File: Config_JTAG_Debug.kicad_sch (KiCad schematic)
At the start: 79 parts, among them J300 DigilentH2SHeader, J301 USB3100-30-A, Q100 T2N7002AK,LM, SW300 SKRPANE010, SW301 219-3LPST, U200 XC7Z010-2CLG400I, U300 FT2232HL, U301 93LC65B-I/SN, X300 ECS-2520MV-120-BN

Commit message: Finished schematic page 4: Zynq Processing System (PS), includes 128MBit QSPI flash, 33.33 MHz PS Clock, and 4Gbyte EMMC Memory
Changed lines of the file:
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@@
     (stroke (width 0) (type default))
   )
-  (wire (pts (xy 21.59 199.39) (xy 36.83 199.39))
+  (wire (pts (xy 35.56 199.39) (xy 36.83 199.39))
     (stroke (width 0) (type default))
   )
@@
     (stroke (width 0) (type default))
   )
-  (wire (pts (xy 91.44 198.12) (xy 105.41 198.12))
+  (wire (pts (xy 104.14 198.12) (xy 105.41 198.12))
     (stroke (width 0) (type default))
   )
@@
     (stroke (width 0) (type default))
   )
-  (wire (pts (xy 21.59 207.01) (xy 36.83 207.01))
+  (wire (pts (xy 35.56 207.01) (xy 36.83 207.01))
     (stroke (width 0) (type default))
   )
@@
     (stroke (width 0) (type default))
   )
-  (wire (pts (xy 21.59 191.77) (xy 36.83 191.77))
+  (wire (pts (xy 35.56 191.77) (xy 36.83 191.77))
     (stroke (width 0) (type default))
   )
@@
     (stroke (width 0) (type default))
   )
-  (wire (pts (xy 138.43 198.12) (xy 153.67 198.12))
+  (wire (pts (xy 152.4 198.12) (xy 153.67 198.12))
     (stroke (width 0) (type default))
   )
@@
     (effects (font (size 1.27 1.27)) (justify right bottom))
   )
-  (label "QSPI_DQ1_M1" (at 21.59 199.39 0) (fields_autoplaced)
-    (effects (font (size 1.27 1.27)) (justify left bottom))
-  )
   (label "M1" (at 45.72 199.39 0) (fields_autoplaced)
     (effects (font (size 1.27 1.27)) (justify left bottom))
@@
     (effects (font (size 1.27 1.27)) (justify left bottom))
   )
-  (label "QSPI_DQ3_M0" (at 21.59 191.77 0) (fields_autoplaced)
-    (effects (font (size 1.27 1.27)) (justify left bottom))
-  )
-  (label "QSPI_DQ2_M2" (at 21.59 207.01 0) (fields_autoplaced)
-    (effects (font (size 1.27 1.27)) (justify left bottom))
-  )
   (label "CLK_12MHZ" (at 238.76 229.87 0) (fields_autoplaced)
     (effects (font (size 1.27 1.27)) (justify left bottom))
@@
     (effects (font (size 1.27 1.27)) (justify left bottom))
   )
-  (label "QSPI_DQ0_M3" (at 91.44 198.12 0) (fields_autoplaced)
-    (effects (font (size 1.27 1.27)) (justify left bottom))
-  )
   (label "TCK" (at 53.34 73.66 0) (fields_autoplaced)
     (effects (font (size 1.27 1.27)) (justify left bottom))
@@
     (effects (font (size 1.27 1.27)) (justify left bottom))
   )
-  (label "FLASH_CLK_M4" (at 138.43 198.12 0) (fields_autoplaced)
-    (effects (font (size 1.27 1.27)) (justify left bottom))
-  )
   (label "JTAG_TDO" (at 153.67 71.12 0) (fields_autoplaced)
     (effects (font (size 0.762 0.762)) (justify left bottom))
@@
     (effects (font (size 1.016 1.016)) (justify left bottom))
   )
+  (global_label "QSPI_DQ1_M1" (shape input) (at 35.56 199.39 180) (fields_autoplaced)
+    (effects (font (size 1.27 1.27)) (justify right))
+    (property "Intersheetrefs" "${INTERSHEET_REFS}" (at 0 0 0)
+      (effects (font (size 1.27 1.27)) hide)
+    )
+  )
   (global_label "UART1_RX" (shape output) (at 387.35 161.29 0) (fields_autoplaced)
     (effects (font (size 1.27 1.27)) (justify left))
+    (property "Intersheetrefs" "${INTERSHEET_REFS}" (at 0 0 0)
+      (effects (font (size 1.27 1.27)) hide)
+    )
+  )
+  (global_label "FLASH_CLK_M4" (shape input) (at 152.4 198.12 180) (fields_autoplaced)
+    (effects (font (size 1.27 1.27)) (justify right))
+    (property "Intersheetrefs" "${INTERSHEET_REFS}" (at 0 0 0)
+      (effects (font (size 1.27 1.27)) hide)
+    )
+  )
+  (global_label "QSPI_DQ2_M2" (shape input) (at 35.56 207.01 180) (fields_autoplaced)
+    (effects (font (size 1.27 1.27)) (justify right))
+    (property "Intersheetrefs" "${INTERSHEET_REFS}" (at 0 0 0)
+      (effects (font (size 1.27 1.27)) hide)
+    )
+  )
+  (global_label "QSPI_DQ0_M3" (shape input) (at 104.14 198.12 180) (fields_autoplaced)
+    (effects (font (size 1.27 1.27)) (justify right))
+    (property "Intersheetrefs" "${INTERSHEET_REFS}" (at 0 0 0)
+      (effects (font (size 1.27 1.27)) hide)
+    )
+  )
+  (global_label "QSPI_DQ3_M0" (shape input) (at 35.56 191.77 180) (fields_autoplaced)
+    (effects (font (size 1.27 1.27)) (justify right))
+    (property "Intersheetrefs" "${INTERSHEET_REFS}" (at 0 0 0)
+      (effects (font (size 1.27 1.27)) hide)
+    )
   )
   (global_label "UART1_TX_VCFG1" (shape input) (at 383.54 166.37 0) (fields_autoplaced)
     (effects (font (size 1.27 1.27)) (justify left))
+    (property "Intersheetrefs" "${INTERSHEET_REFS}" (at 0 0 0)
+      (effects (font (size 1.27 1.27)) hide)
+    )
   )
   (global_label "PS_NPOR" (shape bidirectional) (at 384.81 130.81 0) (fields_autoplaced)
@@
         )
         (path "/ec71d28a-654e-4dfb-b412-dd09b7b3e4b8/b94623a7-025c-4682-97b9-752e423a938a"
-          (reference "C1") (unit 1)
+          (reference "C307") (unit 1)
         )
       )
@@
         )
         (path "/ec71d28a-654e-4dfb-b412-dd09b7b3e4b8/b94623a7-025c-4682-97b9-752e423a938a"
-          (reference "C3") (unit 1)
+          (reference "C309") (unit 1)
         )
       )
@@
         )
         (path "/ec71d28a-654e-4dfb-b412-dd09b7b3e4b8/b94623a7-025c-4682-97b9-752e423a938a"
-          (reference "C2") (unit 1)
+          (reference "C308") (unit 1)
         )
       )
@@
       (effects (font (size 1.27 1.27)) hide)
     )
+    (property "LCSC #" "" (at 29.21 227.33 0)
+      (effects (font (size 1.27 1.27)) hide)
+    )
     (pin "F6")
     (pin "F9")
@@
     (pin "R10")
     (pin "R11")
+    (pin "A10")
+    (pin "A11")
+    (pin "A12")
+    (pin "A14")
+    (pin "A15")
+    (pin "A16")
+    (pin "A17")
+    (pin "A19")
+    (pin "A5")
+    (pin "A6")
+    (pin "A7")
+    (pin "A9")
+    (pin "B10")
+    (pin "B12")
+    (pin "B13")
+    (pin "B14")
+    (pin "B15")
+    (pin "B17")
+    (pin "B18")
+    (pin "B5")
+    (pin "B7")
+    (pin "B8")
+    (pin "B9")
+    (pin "C10")
+    (pin "C11")
+    (pin "C12")
+    (pin "C13")
+    (pin "C15")
+    (pin "C16")
+    (pin "C17")
+    (pin "C18")
+    (pin "C5")
+    (pin "C6")
+    (pin "C7")
+    (pin "C8")
+    (pin "D10")
+    (pin "D11")
+    (pin "D13")
+    (pin "D14")
+    (pin "D15")
+    (pin "D16")
+    (pin "D5")
+    (pin "D6")
+    (pin "D8")
+    (pin "D9")
+    (pin "E11")
+    (pin "E12")
+    (pin "E13")
+    (pin "E14")
+    (pin "E16")
+    (pin "E6")
+    (pin "E7")
+    (pin "E8")
+    (pin "E9")
+    (pin "F12")
+    (pin "F13")
+    (pin "F14")
+    (pin "F15")
     (pin "C19")
     (pin "F18")
@@
         )
         (path "/ec71d28a-654e-4dfb-b412-dd09b7b3e4b8/b94623a7-025c-4682-97b9-752e423a938a"
-          (reference "D1") (unit 1)
+          (reference "D309") (unit 1)
         )
       )
@@
         )
         (path "/ec71d28a-654e-4dfb-b412-dd09b7b3e4b8/b94623a7-025c-4682-97b9-752e423a938a"
-          (reference "D2") (unit 1)
+          (reference "D305") (unit 1)
         )
       )

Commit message: Added page '[7] 1GB DDR3L Modules'
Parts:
- renumbered C120 to C300, C129 to C301, C129 to C302, C129 to C303, C120 to C304, C129 to C305, C120 to C306, C120 to C307, C120 to C308, C120 to C309, C120 to C310, C120 to C311, C120 to C312, C120 to C313, C120 to C314, C129 to C315, C120 to C316, C120 to C318, D101 to D300, D100 to D305, D101 to D308, D101 to D309, FB200 to FB1, FB200 to FB300, FB200 to FB301, Q100 to Q300, R102 to R300, R102 to R301, R102 to R302, R102 to R303, R102 to R304, R102 to R305, R102 to R306, R102 to R307, R102 to R308, R123 to R309, R127 to R310, R127 to R311, R127 to R312, R127 to R313, R127 to R314, R127 to R315, R127 to R316, R127 to R317, R127 to R318, R127 to R319, R127 to R320, R127 to R321, R104 to R322, R104 to R323, R101 to R324, R101 to R325, R101 to R326, R101 to R327, R101 to R328, R102 to R329, R102 to R330, R102 to R331, R102 to R332, R102 to R333, R102 to R334, R102 to R335, R123 to R336, R123 to R337, R102 to R338

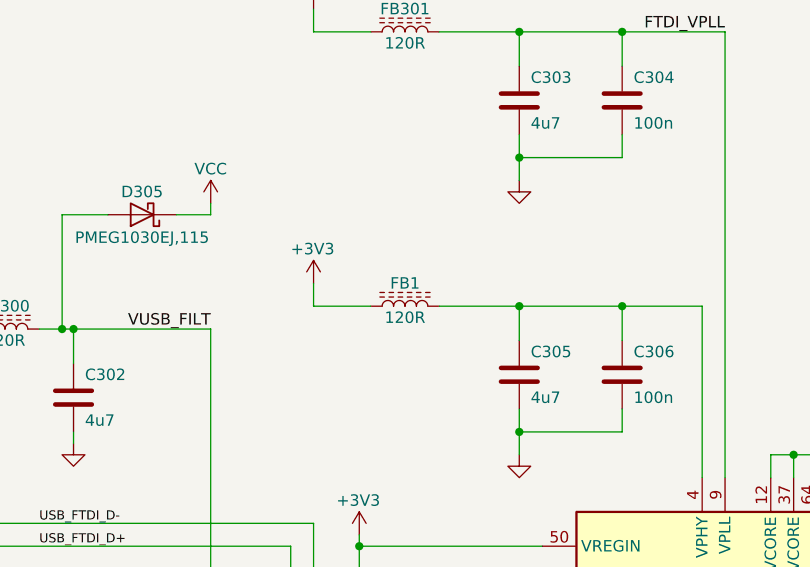
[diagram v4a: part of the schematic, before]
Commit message: Completed page 8, Gigabit Ethernet Controller
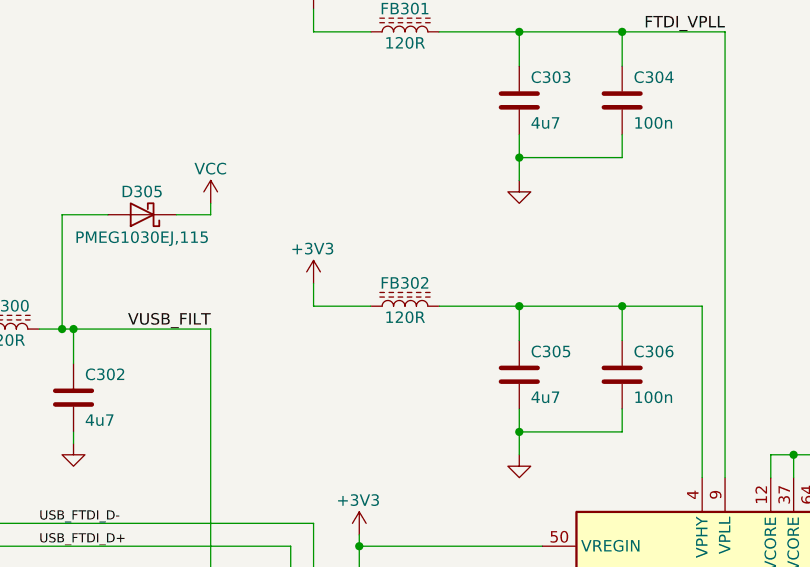
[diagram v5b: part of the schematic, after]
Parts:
- renumbered FB1 to FB302
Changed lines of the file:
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@@
 		(on_board yes)
 		(dnp no)
-		(property "Reference" "FB1"
+		(property "Reference" "FB302"
 			(at 278.13 88.9 90)
 			(effects
@@
 			(project "ZeBra-X"
 				(path "/ec71d28a-654e-4dfb-b412-dd09b7b3e4b8/b94623a7-025c-4682-97b9-752e423a938a"
-					(reference "FB1")
+					(reference "FB302")
 					(unit 1)
 				)

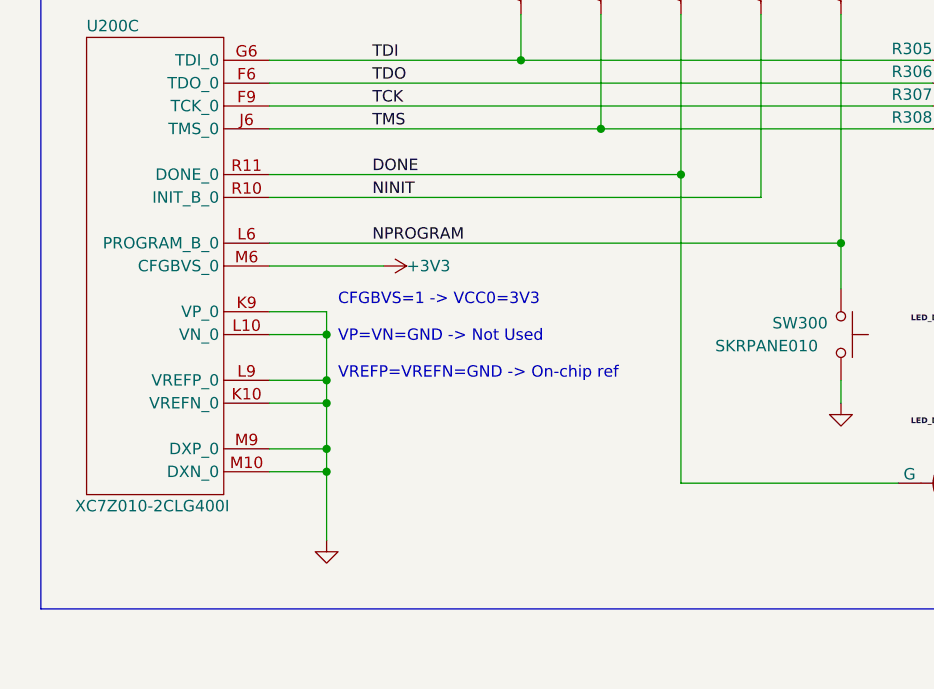
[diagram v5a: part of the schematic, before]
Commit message: Finished first pass of schematic, needs netclass assignments and double check
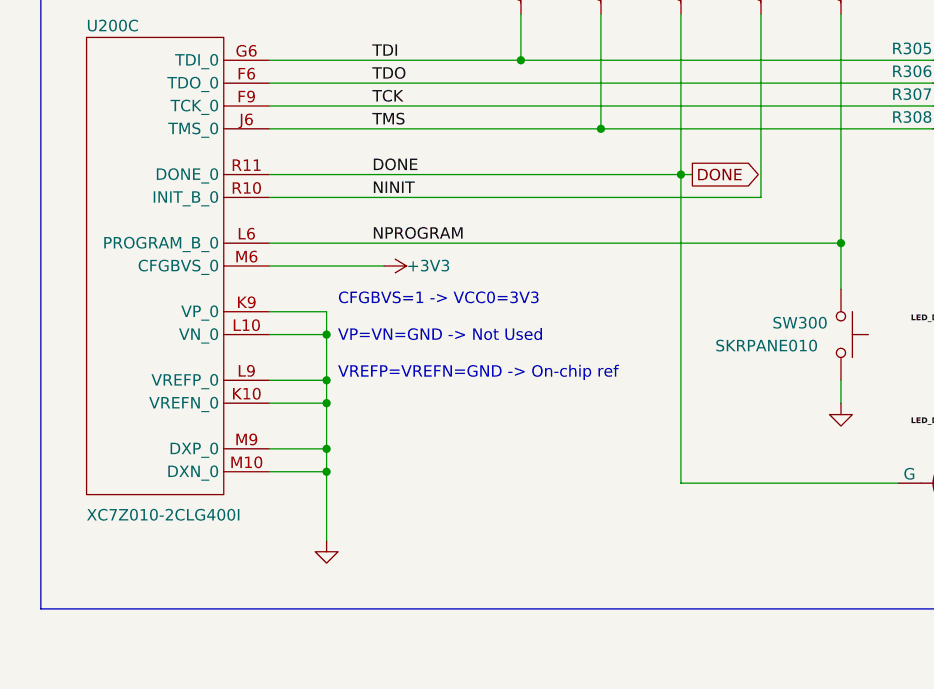
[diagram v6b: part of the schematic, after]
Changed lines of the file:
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@@
 	(wire
 		(pts
+			(xy 87.63 81.28) (xy 88.9 81.28)
+		)
+		(stroke
+			(width 0)
+			(type default)
+		)
+	)
+	(wire
+		(pts
 			(xy 207.01 129.54) (xy 207.01 132.08)
 		)
@@
 		)
 	)
+	(global_label "DONE"
+		(shape output)
+		(at 88.9 81.28 0)
+		(fields_autoplaced yes)
+		(effects
+			(font
+				(size 1.27 1.27)
+			)
+			(justify left)
+		)
+		(property "Intersheetrefs" "${INTERSHEET_REFS}"
+			(at 96.9652 81.28 0)
+			(effects
+				(font
+					(size 1.27 1.27)
+				)
+				(justify left)
+				(hide yes)
+			)
+		)
+	)
 	(symbol
 		(lib_id "Device:R_US")
@@
 		)
 		(property "Value" "XC7Z010-2CLG400I"
-			(at 20.32 118.11 0)
+			(at 21.59 119.126 0)
 			(effects
 				(font
@@
 		)
 		(instances
-			(project "ZeBra-X"
+			(project ""
+				(path "/ec71d28a-654e-4dfb-b412-dd09b7b3e4b8/369d50d7-e508-4bcb-a2d0-a2c7d0c5b870"
+					(reference "U200")
+					(unit 3)
+				)
 				(path "/ec71d28a-654e-4dfb-b412-dd09b7b3e4b8/b94623a7-025c-4682-97b9-752e423a938a"
 					(reference "U200")
